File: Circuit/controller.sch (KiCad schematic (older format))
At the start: 13 parts

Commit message: Updated pcb to start placing components.
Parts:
- C7, C8, C9: renamed from C?; footprint (none) -> Capacitors_SMD:C_0603_HandSoldering
- R10, R11, R12, R14, R7, R8: renamed from R?; footprint (none) -> Resistors_SMD:R_0603_HandSoldering
- SW4, SW6: renamed from SW?; footprint (none) -> freetronics_footprints:SW_PUSHBUTTON_PTH
- U?1: renamed from U??; footprint FT:JOYSTICK_W_BUTTON -> freetronics_footprints:JOYSTICK_W_BUTTON
- gave numbers to parts that had none: 1
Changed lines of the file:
@@
 LIBS:cp2102
 LIBS:ltc3426
-LIBS:rotary
 LIBS:adxl345
 LIBS:bme280
@@
 $EndDescr
 $Comp
-L JOYSTICK_W_BUTTON U??
+L JOYSTICK_W_BUTTON U?1
 U 1 1 58137DE7
 P 1800 1450
-F 0 "U??" H 2000 1000 60  0000 C CNN
+F 0 "U?1" H 2000 1000 60  0000 C CNN
 F 1 "JOYSTICK_W_BUTTON" H 1800 1100 30  0000 C CNN
-F 2 "FT:JOYSTICK_W_BUTTON" H 1800 1450 60  0001 C CNN
+F 2 "freetronics_footprints:JOYSTICK_W_BUTTON" H 1800 1450 60  0001 C CNN
 F 3 "" H 1900 850 60  0000 C CNN
 	1    1800 1450
@@
 $EndComp
 $Comp
-L R R?
+L R R7
 U 1 1 58137E6F
 P 950 1050
-F 0 "R?" V 1030 1050 50  0000 C CNN
+F 0 "R7" V 1030 1050 50  0000 C CNN
 F 1 "470R(1%)" V 850 1050 50  0000 C CNN
-F 2 "" V 880 1050 50  0000 C CNN
+F 2 "Resistors_SMD:R_0603_HandSoldering" V 880 1050 50  0001 C CNN
 F 3 "" H 950 1050 50  0000 C CNN
 	1    950  1050
@@
 $EndComp
 $Comp
-L C C?
+L C C7
 U 1 1 58137EF2
 P 950 1450
-F 0 "C?" H 975 1550 50  0000 L CNN
+F 0 "C7" H 975 1550 50  0000 L CNN
 F 1 "1nF" H 975 1350 50  0000 L CNN
-F 2 "" H 988 1300 50  0000 C CNN
+F 2 "Capacitors_SMD:C_0603_HandSoldering" H 988 1300 50  0001 C CNN
 F 3 "" H 950 1450 50  0000 C CNN
 	1    950  1450
@@
 $EndComp
 $Comp
-L GND #PWR?
+L GND #PWR048
 U 1 1 58137F56
 P 950 1750
-F 0 "#PWR?" H 950 1500 50  0001 C CNN
+F 0 "#PWR048" H 950 1500 50  0001 C CNN
 F 1 "GND" H 950 1600 50  0000 C CNN
 F 2 "" H 950 1750 50  0000 C CNN
@@
 $EndComp
 $Comp
-L +3.3V #PWR?
+L +3.3V #PWR049
 U 1 1 58137F70
 P 1700 850
-F 0 "#PWR?" H 1700 700 50  0001 C CNN
+F 0 "#PWR049" H 1700 700 50  0001 C CNN
 F 1 "+3.3V" H 1700 990 50  0000 C CNN
 F 2 "" H 1700 850 50  0000 C CNN
@@
 	2050 950  2050 1000
 $Comp
-L GND #PWR?
+L GND #PWR050
 U 1 1 581380AB
 P 2050 1000
-F 0 "#PWR?" H 2050 750 50  0001 C CNN
+F 0 "#PWR050" H 2050 750 50  0001 C CNN
 F 1 "GND" H 2050 850 50  0000 C CNN
 F 2 "" H 2050 1000 50  0000 C CNN
@@
 	2450 1350 2450 1300
 $Comp
-L GND #PWR?
+L GND #PWR051
 U 1 1 58138157
 P 2450 1600
-F 0 "#PWR?" H 2450 1350 50  0001 C CNN
+F 0 "#PWR051" H 2450 1350 50  0001 C CNN
 F 1 "GND" H 2450 1450 50  0000 C CNN
 F 2 "" H 2450 1600 50  0000 C CNN
@@
 $EndComp
 $Comp
-L +3.3V #PWR?
+L +3.3V #PWR052
 U 1 1 5813816B
 P 2450 1300
-F 0 "#PWR?" H 2450 1150 50  0001 C CNN
+F 0 "#PWR052" H 2450 1150 50  0001 C CNN
 F 1 "+3.3V" H 2450 1440 50  0000 C CNN
 F 2 "" H 2450 1300 50  0000 C CNN
@@
 	950  850  1000 850
 $Comp
-L SW_PUSH SW?
+L SW_PUSH SW4
 U 1 1 5813BF62
 P 4950 1300
-F 0 "SW?" H 5100 1410 50  0000 C CNN
+F 0 "SW4" H 5100 1410 50  0000 C CNN
 F 1 "A" H 4950 1220 50  0000 C CNN
-F 2 "" H 4950 1300 50  0000 C CNN
+F 2 "freetronics_footprints:SW_PUSHBUTTON_PTH" H 4950 1300 50  0001 C CNN
 F 3 "" H 4950 1300 50  0000 C CNN
 	1    4950 1300
@@
 $EndComp
 $Comp
-L C C?
+L C C8
 U 1 1 5813BFC7
 P 5200 1300
-F 0 "C?" H 5225 1400 50  0000 L CNN
+F 0 "C8" H 5225 1400 50  0000 L CNN
 F 1 "1nF" H 5225 1200 50  0000 L CNN
-F 2 "" H 5238 1150 50  0000 C CNN
+F 2 "Capacitors_SMD:C_0603_HandSoldering" H 5238 1150 50  0001 C CNN
 F 3 "" H 5200 1300 50  0000 C CNN
 	1    5200 1300
@@
 $EndComp
 $Comp
-L R R?
+L R R12
 U 1 1 5813BFFC
 P 5450 1000
-F 0 "R?" V 5530 1000 50  0000 C CNN
+F 0 "R12" V 5530 1000 50  0000 C CNN
 F 1 "470R(1%)" V 5350 1000 50  0000 C CNN
-F 2 "" V 5380 1000 50  0000 C CNN
+F 2 "Resistors_SMD:R_0603_HandSoldering" V 5380 1000 50  0001 C CNN
 F 3 "" H 5450 1000 50  0000 C CNN
 	1    5450 1000
@@
 $EndComp
 $Comp
-L GND #PWR?
+L GND #PWR053
 U 1 1 5813C06B
 P 4950 1700
-F 0 "#PWR?" H 4950 1450 50  0001 C CNN
+F 0 "#PWR053" H 4950 1450 50  0001 C CNN
 F 1 "GND" H 4950 1550 50  0000 C CNN
 F 2 "" H 4950 1700 50  0000 C CNN
@@
 Connection ~ 5200 1000
 $Comp
-L SW_PUSH SW?
+L SW_PUSH SW6
 U 1 1 5813C2D7
 P 4950 2350
-F 0 "SW?" H 5100 2460 50  0000 C CNN
+F 0 "SW6" H 5100 2460 50  0000 C CNN
 F 1 "B" H 4950 2270 50  0000 C CNN
-F 2 "" H 4950 2350 50  0000 C CNN
+F 2 "freetronics_footprints:SW_PUSHBUTTON_PTH" H 4950 2350 50  0001 C CNN
 F 3 "" H 4950 2350 50  0000 C CNN
 	1    4950 2350
@@
 $EndComp
 $Comp
-L C C?
+L C C9
 U 1 1 5813C2DD
 P 5200 2350
-F 0 "C?" H 5225 2450 50  0000 L CNN
+F 0 "C9" H 5225 2450 50  0000 L CNN
 F 1 "1nF" H 5225 2250 50  0000 L CNN
-F 2 "" H 5238 2200 50  0000 C CNN
+F 2 "Capacitors_SMD:C_0603_HandSoldering" H 5238 2200 50  0001 C CNN
 F 3 "" H 5200 2350 50  0000 C CNN
 	1    5200 2350
@@
 $EndComp
 $Comp
-L R R?
+L R R14
 U 1 1 5813C2E3
 P 5450 2050
-F 0 "R?" V 5530 2050 50  0000 C CNN
+F 0 "R14" V 5530 2050 50  0000 C CNN
 F 1 "470R(1%)" V 5350 2050 50  0000 C CNN
-F 2 "" V 5380 2050 50  0000 C CNN
+F 2 "Resistors_SMD:R_0603_HandSoldering" V 5380 2050 50  0001 C CNN
 F 3 "" H 5450 2050 50  0000 C CNN
 	1    5450 2050
@@
 $EndComp
 $Comp
-L GND #PWR?
+L GND #PWR054
 U 1 1 5813C2E9
 P 4950 2750
-F 0 "#PWR?" H 4950 2500 50  0001 C CNN
+F 0 "#PWR054" H 4950 2500 50  0001 C CNN
 F 1 "GND" H 4950 2600 50  0000 C CNN
 F 2 "" H 4950 2750 50  0000 C CNN
@@
 B_BUTTON
 $Comp
-L ROTARY_ENCODER_SWITCH SW?
+L ROTARY_ENCODER_SWITCH SW2
 U 1 1 58141638
 P 2200 3750
-F 0 "SW?" H 2200 4010 50  0000 C CNN
+F 0 "SW2" H 2200 4010 50  0000 C CNN
 F 1 "ROTARY_ENCODER_SWITCH" H 2200 3490 50  0000 C CNN
 F 2 "" H 2100 3910 50  0001 C CNN
@@
 $EndComp
 $Comp
-L GND #PWR?
+L GND #PWR055
 U 1 1 58141715
 P 1550 3950
-F 0 "#PWR?" H 1550 3700 50  0001 C CNN
+F 0 "#PWR055" H 1550 3700 50  0001 C CNN
 F 1 "GND" H 1550 3800 50  0000 C CNN
 F 2 "" H 1550 3950 50  0000 C CNN
@@
 $EndComp
 $Comp
-L R R?
+L R R10
 U 1 1 58141771
 P 1500 3550
-F 0 "R?" V 1580 3550 50  0000 C CNN
+F 0 "R10" V 1580 3550 50  0000 C CNN
 F 1 "10K" V 1400 3550 50  0000 C CNN
-F 2 "" V 1430 3550 50  0000 C CNN
+F 2 "Resistors_SMD:R_0603_HandSoldering" V 1430 3550 50  0001 C CNN
 F 3 "" H 1500 3550 50  0000 C CNN
 	1    1500 3550
@@
 	1550 3750 1900 3750
 $Comp
-L GND #PWR?
+L GND #PWR056
 U 1 1 58141924
 P 2800 3950
-F 0 "#PWR?" H 2800 3700 50  0001 C CNN
+F 0 "#PWR056" H 2800 3700 50  0001 C CNN
 F 1 "GND" H 2800 3800 50  0000 C CNN
 F 2 "" H 2800 3950 50  0000 C CNN
@@
 	2800 3850 2500 3850
 $Comp
-L R R?
+L R R11
 U 1 1 58141984
 P 2750 3650
-F 0 "R?" V 2830 3650 50  0000 C CNN
+F 0 "R11" V 2830 3650 50  0000 C CNN
 F 1 "10K" V 2650 3650 50  0000 C CNN
-F 2 "" V 2680 3650 50  0000 C CNN
+F 2 "Resistors_SMD:R_0603_HandSoldering" V 2680 3650 50  0001 C CNN
 F 3 "" H 2750 3650 50  0000 C CNN
 	1    2750 3650
@@
 $EndComp
 $Comp
-L +3.3V #PWR?
+L +3.3V #PWR057
 U 1 1 58141A8C
 P 3000 3550
-F 0 "#PWR?" H 3000 3400 50  0001 C CNN
+F 0 "#PWR057" H 3000 3400 50  0001 C CNN
 F 1 "+3.3V" H 3000 3690 50  0000 C CNN
 F 2 "" H 3000 3550 50  0000 C CNN
@@
 	2550 3300 2550 3650
 $Comp
-L R R?
+L R R8
 U 1 1 58141E89
 P 1500 3200
-F 0 "R?" V 1580 3200 50  0000 C CNN
+F 0 "R8" V 1580 3200 50  0000 C CNN
 F 1 "10K" V 1400 3200 50  0000 C CNN
-F 2 "" V 1430 3200 50  0000 C CNN
+F 2 "Resistors_SMD:R_0603_HandSoldering" V 1430 3200 50  0001 C CNN
 F 3 "" H 1500 3200 50  0000 C CNN
 	1    1500 3200
@@
 $EndComp
 $Comp
-L +3.3V #PWR?
+L +3.3V #PWR058
 U 1 1 58141FF1
 P 1250 3100
-F 0 "#PWR?" H 1250 2950 50  0001 C CNN
+F 0 "#PWR058" H 1250 2950 50  0001 C CNN
 F 1 "+3.3V" H 1250 3240 50  0000 C CNN
 F 2 "" H 1250 3100 50  0000 C CNN

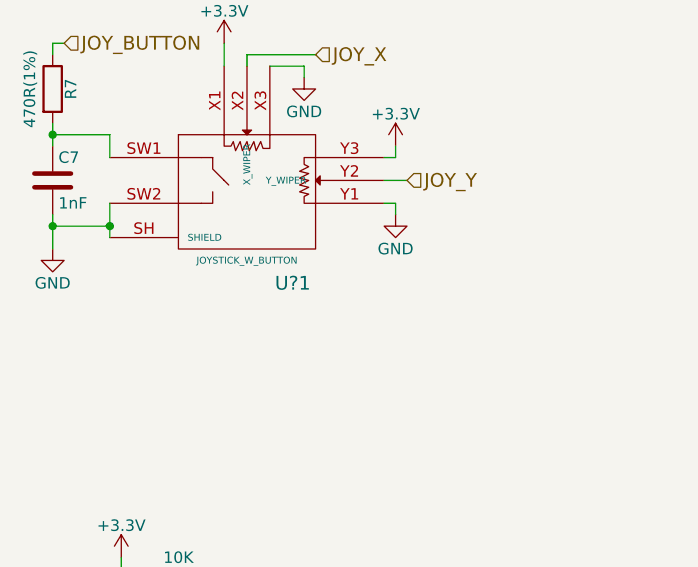
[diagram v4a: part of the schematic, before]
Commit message: Added EC11 Rotary Encoder footprint
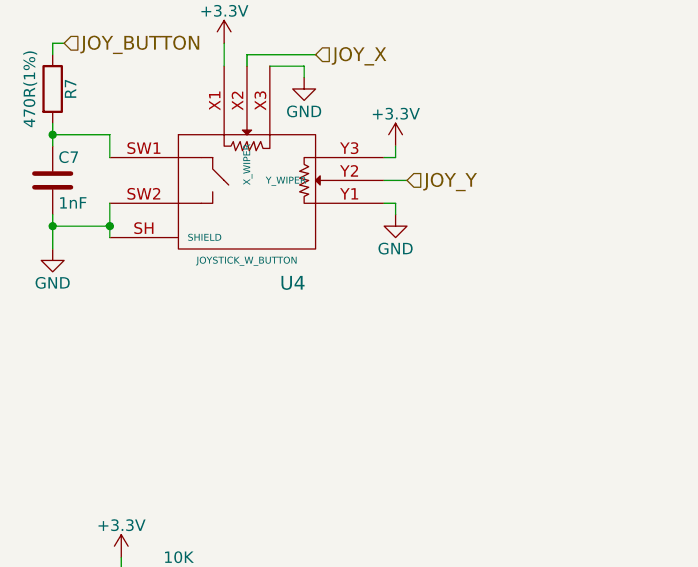
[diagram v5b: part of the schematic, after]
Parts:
- SW2: footprint (none) -> libs:EC11
- renumbered U?1 to U4
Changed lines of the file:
@@
 $EndDescr
 $Comp
-L JOYSTICK_W_BUTTON U?1
+L JOYSTICK_W_BUTTON U4
 U 1 1 58137DE7
 P 1800 1450
-F 0 "U?1" H 2000 1000 60  0000 C CNN
+F 0 "U4" H 2000 1000 60  0000 C CNN
 F 1 "JOYSTICK_W_BUTTON" H 1800 1100 30  0000 C CNN
 F 2 "freetronics_footprints:JOYSTICK_W_BUTTON" H 1800 1450 60  0001 C CNN
@@
 $EndComp
 $Comp
-L GND #PWR47
+L GND #PWR049
 U 1 1 58137F56
 P 950 1750
-F 0 "#PWR47" H 950 1500 50  0001 C CNN
+F 0 "#PWR049" H 950 1500 50  0001 C CNN
 F 1 "GND" H 950 1600 50  0000 C CNN
 F 2 "" H 950 1750 50  0000 C CNN
@@
 $EndComp
 $Comp
-L +3.3V #PWR50
+L +3.3V #PWR050
 U 1 1 58137F70
 P 1700 850
-F 0 "#PWR50" H 1700 700 50  0001 C CNN
+F 0 "#PWR050" H 1700 700 50  0001 C CNN
 F 1 "+3.3V" H 1700 990 50  0000 C CNN
 F 2 "" H 1700 850 50  0000 C CNN
@@
 	2050 950  2050 1000
 $Comp
-L GND #PWR51
+L GND #PWR051
 U 1 1 581380AB
 P 2050 1000
-F 0 "#PWR51" H 2050 750 50  0001 C CNN
+F 0 "#PWR051" H 2050 750 50  0001 C CNN
 F 1 "GND" H 2050 850 50  0000 C CNN
 F 2 "" H 2050 1000 50  0000 C CNN
@@
 	2450 1350 2450 1300
 $Comp
-L GND #PWR53
+L GND #PWR052
 U 1 1 58138157
 P 2450 1600
-F 0 "#PWR53" H 2450 1350 50  0001 C CNN
+F 0 "#PWR052" H 2450 1350 50  0001 C CNN
 F 1 "GND" H 2450 1450 50  0000 C CNN
 F 2 "" H 2450 1600 50  0000 C CNN
@@
 $EndComp
 $Comp
-L +3.3V #PWR52
+L +3.3V #PWR053
 U 1 1 5813816B
 P 2450 1300
-F 0 "#PWR52" H 2450 1150 50  0001 C CNN
+F 0 "#PWR053" H 2450 1150 50  0001 C CNN
 F 1 "+3.3V" H 2450 1440 50  0000 C CNN
 F 2 "" H 2450 1300 50  0000 C CNN
@@
 $EndComp
 $Comp
-L GND #PWR56
+L GND #PWR054
 U 1 1 5813C06B
 P 4950 1700
-F 0 "#PWR56" H 4950 1450 50  0001 C CNN
+F 0 "#PWR054" H 4950 1450 50  0001 C CNN
 F 1 "GND" H 4950 1550 50  0000 C CNN
 F 2 "" H 4950 1700 50  0000 C CNN
@@
 $EndComp
 $Comp
-L GND #PWR57
+L GND #PWR055
 U 1 1 5813C2E9
 P 4950 2750
-F 0 "#PWR57" H 4950 2500 50  0001 C CNN
+F 0 "#PWR055" H 4950 2500 50  0001 C CNN
 F 1 "GND" H 4950 2600 50  0000 C CNN
 F 2 "" H 4950 2750 50  0000 C CNN
@@
 F 0 "SW2" H 2200 4010 50  0000 C CNN
 F 1 "ROTARY_ENCODER_SWITCH" H 2200 3490 50  0000 C CNN
-F 2 "" H 2100 3910 50  0001 C CNN
+F 2 "libs:EC11" H 2100 3910 50  0001 C CNN
 F 3 "" H 2200 4010 50  0001 C CNN
 	1    2200 3750
@@
 $EndComp
 $Comp
-L GND #PWR49
+L GND #PWR056
 U 1 1 58141715
 P 1550 3950
-F 0 "#PWR49" H 1550 3700 50  0001 C CNN
+F 0 "#PWR056" H 1550 3700 50  0001 C CNN
 F 1 "GND" H 1550 3800 50  0000 C CNN
 F 2 "" H 1550 3950 50  0000 C CNN
@@
 	1550 3750 1900 3750
 $Comp
-L GND #PWR54
+L GND #PWR057
 U 1 1 58141924
 P 2800 3950
-F 0 "#PWR54" H 2800 3700 50  0001 C CNN
+F 0 "#PWR057" H 2800 3700 50  0001 C CNN
 F 1 "GND" H 2800 3800 50  0000 C CNN
 F 2 "" H 2800 3950 50  0000 C CNN
@@
 $EndComp
 $Comp
-L +3.3V #PWR55
+L +3.3V #PWR058
 U 1 1 58141A8C
 P 3000 3550
-F 0 "#PWR55" H 3000 3400 50  0001 C CNN
+F 0 "#PWR058" H 3000 3400 50  0001 C CNN
 F 1 "+3.3V" H 3000 3690 50  0000 C CNN
 F 2 "" H 3000 3550 50  0000 C CNN
@@
 $EndComp
 $Comp
-L +3.3V #PWR48
+L +3.3V #PWR059
 U 1 1 58141FF1
 P 1250 3100
-F 0 "#PWR48" H 1250 2950 50  0001 C CNN
+F 0 "#PWR059" H 1250 2950 50  0001 C CNN
 F 1 "+3.3V" H 1250 3240 50  0000 C CNN
 F 2 "" H 1250 3100 50  0000 C CNN
